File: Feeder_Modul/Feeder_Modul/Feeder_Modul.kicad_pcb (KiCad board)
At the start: 2 copper layers, 156.6 x 125.2 mm, 99 parts, among them J1 Conn_02x01, J101 Conn_02x01, J102 Conn_01x06_Male, J103 Conn_02x01, J104 Conn_02x01, J105 Conn_02x01, J106 USB_A, J107 Conn_02x07_Odd_Even, J108 Conn_02x01, J109 Conn_02x01, Q101 BC847, SW101 SW_Push, SW102 SW_Push, SW103 SW_Push, SW104 SW_Push, SW105 SW_Push, U1 TPS560430, U101 TPS560430, U102 STM32F105R8Tx, U103 M24C01-WMN, U104 EE-SX1350_PCB, U105 DRV8835, U107 SN65HVD230, Y101 48MHz

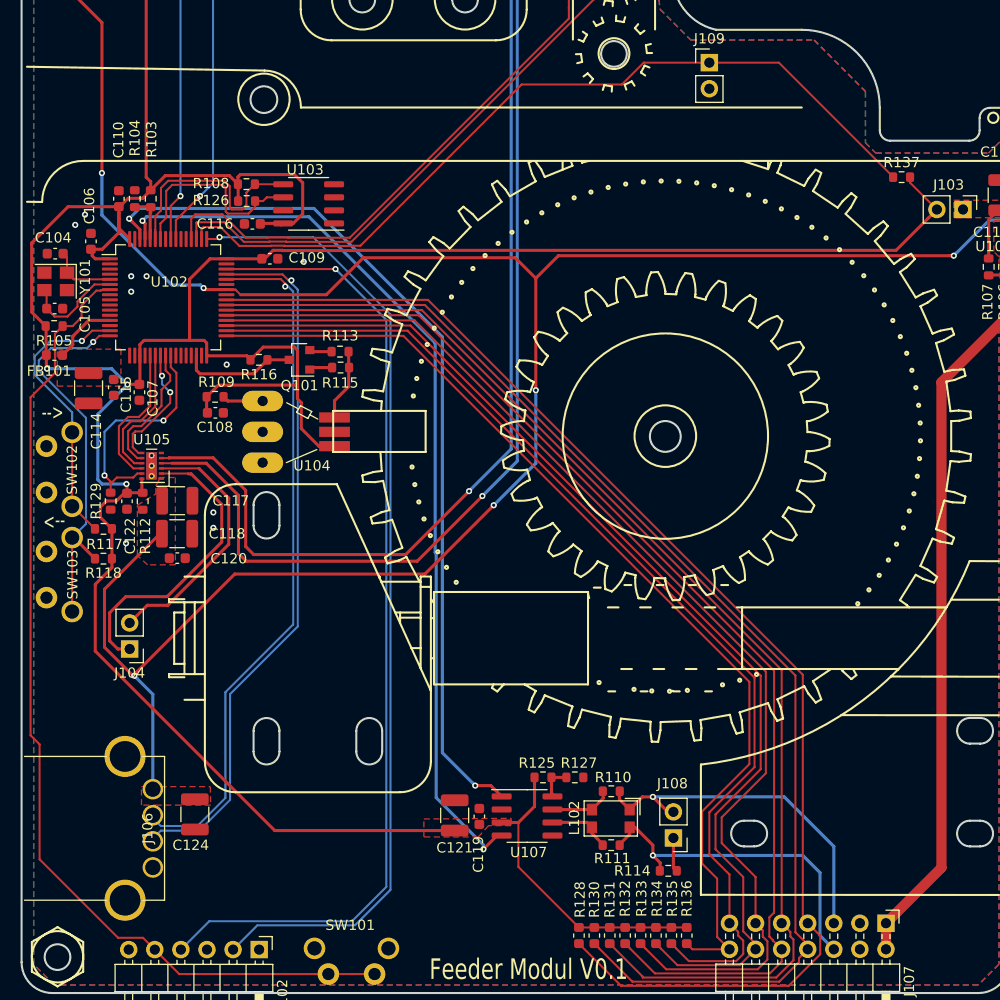
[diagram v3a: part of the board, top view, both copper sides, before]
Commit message: Controller Modul geroutet
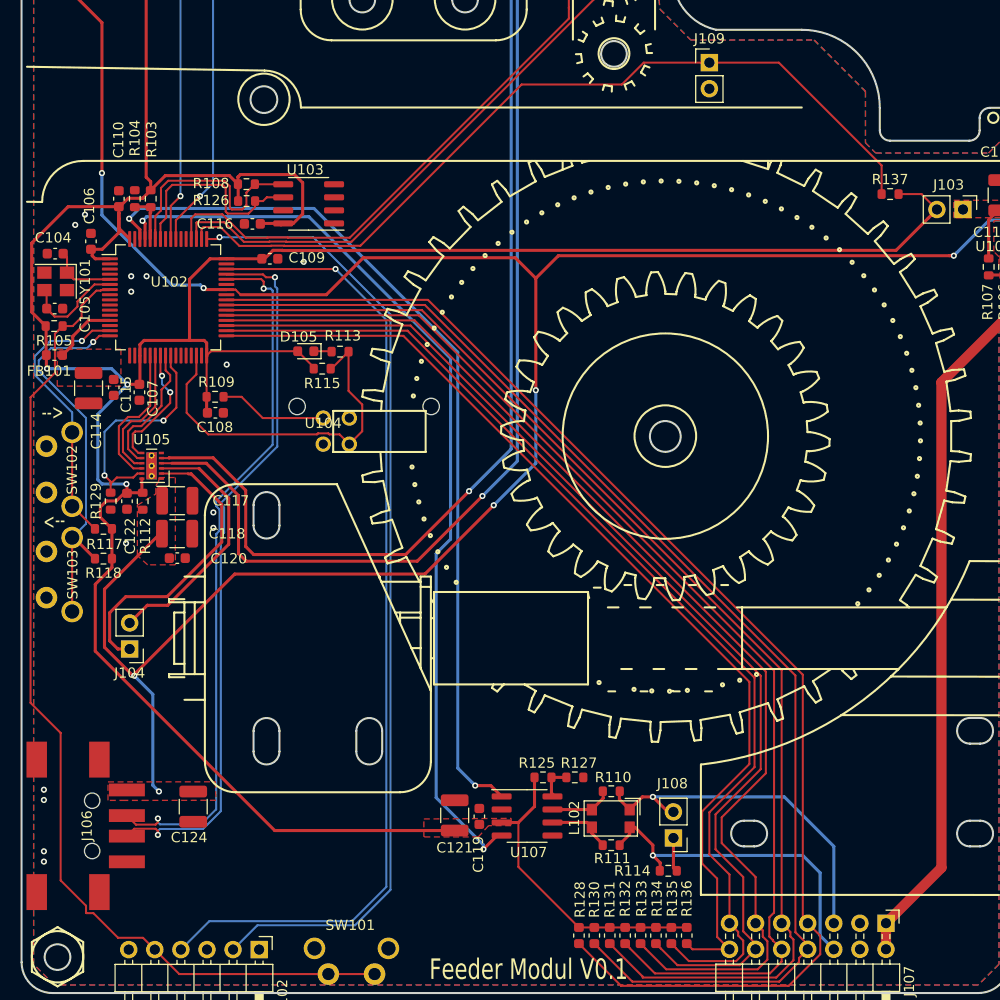
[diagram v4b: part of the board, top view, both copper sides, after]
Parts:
- removed Q101: BC847, Package_TO_SOT_SMD:SOT-23
- removed R116: 10K, Resistor_SMD:R_0603_1608Metric
- added D105: LED_Blue, LED_SMD:LED_0603_1608Metric, F.Cu at (91.5, 98.3)
- J106: value USB_A -> WE_629104190121; footprint ProjectFootprints:USB-A-Conn_LCSC -> ProjectFootprints:WE629104190121
- R113: value 10K -> 1K
- R115: value 1k -> 10K
- U104: value EE-SX1350_PCB -> TCST5250; footprint ProjectFootprints:EE-SX1350_90deg -> ProjectFootprints:TCST5250
- moved J106 5.91 mm to (70.7, 144.5)
- moved U104 2.75 mm to (93.2, 104.8)
- moved R137 1.99 mm to (148.4, 83.0)
- moved R115 1.79 mm to (93.1, 100.0), turned to 180 degrees
- moved C124 0.77 mm to (80.5, 142.7)
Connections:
- R113 pad 1: Net-(R113-Pad1) -> /ENC_OUT
- R113 pad 2: GND -> Net-(D105-Pad1)
- R115 pad 1: Net-(Q101-Pad1) -> /ENC_OUT
- R115 pad 2: Net-(R113-Pad1) -> +3V3
- U104 pad 2: (no net) -> GND
- U104 pad 4: +3V3 -> /ENC_OUT
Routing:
- net /ENC_OUT: track 11.2 -> 35.7 mm
- net +3V3: track 365.8 -> 350.6 mm
- net Net-(R113-Pad1): track 7.33 -> 0.00 mm
- net Net-(R109-Pad1): track 3.97 -> 10.6 mm
- net Net-(Q101-Pad1): track 2.30 -> 0.00 mm
- net GND: track 16.6 -> 14.4 mm, vias 10 -> 14
- net Net-(D105-Pad1): track 0.00 -> 1.74 mm
- net /USB_OTG+: track 69.2 -> 70.6 mm, vias 1 -> 2
- net /USB_OTG-: track 67.7 -> 69.0 mm, vias 1 -> 2
- net /TAPE_MICROBTN: track 81.2 -> 82.4 mm
- net /CAN1_RX: track 89.2 -> 90.4 mm
- net +5V: track 255.9 -> 255.6 mm, vias 6 -> 7

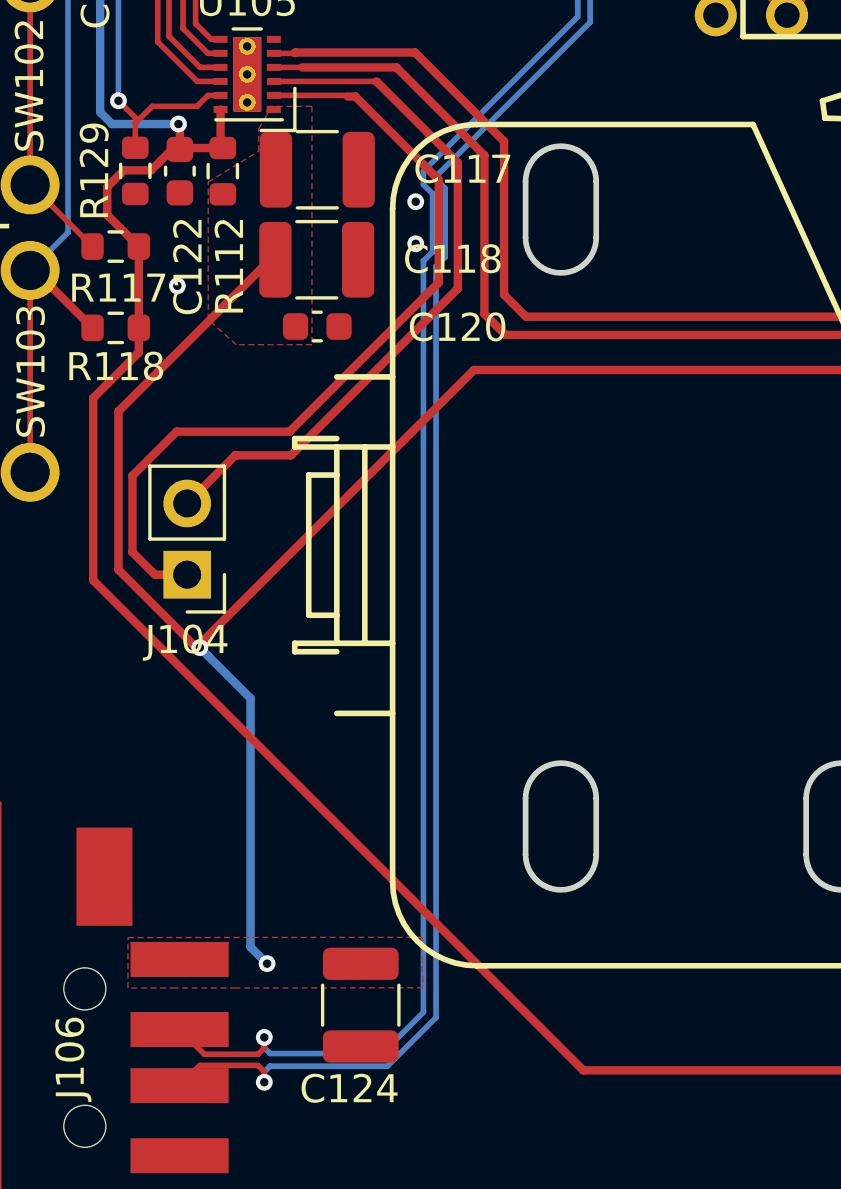
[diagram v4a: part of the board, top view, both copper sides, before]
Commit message: Leere Symbole mit leeren Footprints hinzugefügt für BOM export
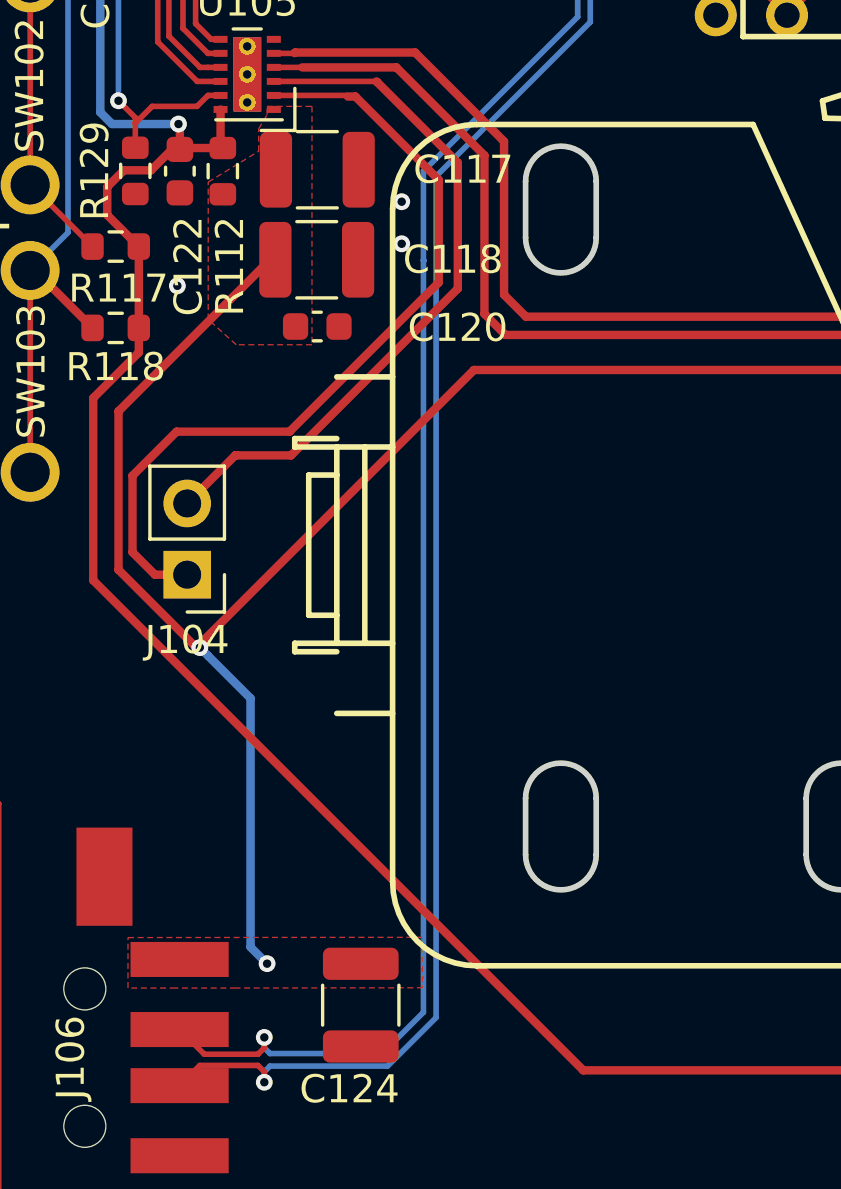
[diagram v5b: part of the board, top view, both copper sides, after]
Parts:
- added U106: Panasonic_ESE22, ProjectFootprints:Empty, F.Cu at (148.0, 138.0)
- added U108: N20_DC_Motor, ProjectFootprints:Empty, F.Cu at (148.0, 139.5)
- added U109: N20_DC_Motor, ProjectFootprints:Empty, F.Cu at (148.0, 141.0)
- R127: value 10K -> 1k
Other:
- board text added: "Empty Footprints for BOM"
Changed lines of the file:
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@@
   (general
     (thickness 1.6)
-    (drawings 1710)
-    (tracks 757)
+    (drawings 1711)
+    (tracks 751)
     (zones 0)
-    (modules 98)
+    (modules 101)
     (nets 66)
   )
@@
   )
   (setup
-    (last_trace_width 0.2)
+    (last_trace_width 0.3)
     (user_trace_width 0.2)
     (user_trace_width 0.3)
@@
     (add_net /MODE)
     (add_net /NRST)
+    (add_net /PA10)
     (add_net /PA13)
     (add_net /PA14)
     (add_net /PA6)
     (add_net /PA7)
+    (add_net /PA8)
     (add_net /PD0)
     (add_net /PD1)
@@
     (add_net "Net-(D104-Pad2)")
     (add_net "Net-(D105-Pad1)")
+    (add_net "Net-(J102-Pad6)")
     (add_net "Net-(J108-Pad1)")
     (add_net "Net-(L102-Pad1)")
@@
     (add_net "Net-(R125-Pad1)")
     (add_net "Net-(R3-Pad2)")
+    (add_net "Net-(U102-Pad10)")
+    (add_net "Net-(U102-Pad11)")
+    (add_net "Net-(U102-Pad14)")
+    (add_net "Net-(U102-Pad17)")
+    (add_net "Net-(U102-Pad2)")
+    (add_net "Net-(U102-Pad20)")
+    (add_net "Net-(U102-Pad26)")
+    (add_net "Net-(U102-Pad27)")
+    (add_net "Net-(U102-Pad28)")
+    (add_net "Net-(U102-Pad29)")
+    (add_net "Net-(U102-Pad3)")
+    (add_net "Net-(U102-Pad4)")
+    (add_net "Net-(U102-Pad53)")
+    (add_net "Net-(U102-Pad54)")
+    (add_net "Net-(U102-Pad57)")
+    (add_net "Net-(U102-Pad8)")
+    (add_net "Net-(U102-Pad9)")
+    (add_net "Net-(U107-Pad5)")
+  )
+  (module ProjectFootprints:Empty (layer F.Cu)
+    (at 148 141)
+    (fp_text reference U109 (at -0.5 -1.25) (layer F.SilkS) hide
+      (effects (font (size 1 1) (thickness 0.15)))
+    )
+    (fp_text value N20_DC_Motor (at -0.5 -1.5) (layer F.Fab)
+      (effects (font (size 1 1) (thickness 0.15)))
+    )
+    (fp_line (start 0 0) (end 1 0) (layer Dwgs.User) (width 0.12))
+  )
+  (module ProjectFootprints:Empty (layer F.Cu)
+    (at 148 139.5)
+    (fp_text reference U108 (at -0.5 -1.25) (layer F.SilkS) hide
+      (effects (font (size 1 1) (thickness 0.15)))
+    )
+    (fp_text value N20_DC_Motor (at -0.5 -1.5) (layer F.Fab)
+      (effects (font (size 1 1) (thickness 0.15)))
+    )
+    (fp_line (start 0 0) (end 1 0) (layer Dwgs.User) (width 0.12))
+  )
+  (module ProjectFootprints:Empty (layer F.Cu)
+    (at 148 138)
+    (fp_text reference U106 (at -0.5 -1.25) (layer F.SilkS) hide
+      (effects (font (size 1 1) (thickness 0.15)))
+    )
+    (fp_text value Panasonic_ESE22 (at -0.5 -1.5) (layer F.Fab)
+      (effects (font (size 1 1) (thickness 0.15)))
+    )
+    (fp_line (start 0 0) (end 1 0) (layer Dwgs.User) (width 0.12))
   )
   (module Resistor_SMD:R_0603_1608Metric (layer F.Cu)
@@
       (effects (font (size 1 1) (thickness 0.15)))
     )
-    (fp_text user %R (at 0 0) (layer F.Fab)
-      (effects (font (size 0.4 0.4) (thickness 0.06)))
-    )
     (fp_line (start -0.8 0.4125) (end -0.8 -0.4125) (layer F.Fab) (width 0.1))
     (fp_line (start -0.8 -0.4125) (end 0.8 -0.4125) (layer F.Fab) (width 0.1))
@@
     (fp_line (start 1.48 -0.73) (end 1.48 0.73) (layer F.CrtYd) (width 0.05))
     (fp_line (start 1.48 0.73) (end -1.48 0.73) (layer F.CrtYd) (width 0.05))
+    (fp_text user %R (at 0 0) (layer F.Fab)
+      (effects (font (size 0.4 0.4) (thickness 0.06)))
+    )
     (pad 2 smd roundrect (at 0.825 0 180) (size 0.8 0.95) (layers F.Cu F.Paste F.Mask) (roundrect_rratio 0.25)
       (net 6 +3V3))
@@
       (effects (font (size 1 1) (thickness 0.15)))
     )
+    (fp_line (start -6.55 6.9) (end 6.55 6.9) (layer Dwgs.User) (width 0.12))
     (fp_text user "Würth PCB Edge" (at -0.3 6.3 90) (layer Dwgs.User)
       (effects (font (size 1 1) (thickness 0.15)))
     )
-    (fp_line (start -6.55 6.9) (end 6.55 6.9) (layer Dwgs.User) (width 0.12))
     (pad 5 smd rect (at -6.45 5.4 270) (size 3.5 2) (layers F.Cu F.Paste F.Mask)
       (net 1 GND))
@@
       (effects (font (size 1 1) (thickness 0.15)))
     )
-    (fp_text value 10K (at 0 1.43) (layer F.Fab)
+    (fp_text value 1k (at 0 1.43) (layer F.Fab)
       (effects (font (size 1 1) (thickness 0.15)))
     )
@@
     )
   )
+  (gr_text "Empty Footprints \nfor BOM" (at 157 140) (layer Dwgs.User)
+    (effects (font (size 1 1) (thickness 0.15)))
+  )
   (gr_circle (center 126.5 106.6) (end 150.7 112.2) (layer Cmts.User) (width 0.15))
   (gr_text "Feeder Modul V0.1" (at 113.2 158.5) (layer F.SilkS)
@@
   (via (at 69.05 86) (size 0.6) (drill 0.3) (layers F.Cu B.Cu) (net 1))
   (via (at 74 117) (size 0.6) (drill 0.3) (layers F.Cu B.Cu) (net 1))
-  (via (at 82.5 114) (size 0.6) (drill 0.3) (layers F.Cu B.Cu) (net 1))
-  (via (at 82.5 115.5) (size 0.6) (drill 0.3) (layers F.Cu B.Cu) (net 1))
+  (via (at 82 114) (size 0.6) (drill 0.3) (layers F.Cu B.Cu) (net 1))
+  (via (at 82 115.5) (size 0.6) (drill 0.3) (layers F.Cu B.Cu) (net 1))
   (via (at 74.5 91) (size 0.6) (drill 0.3) (layers F.Cu B.Cu) (net 1))
   (via (at 76 91) (size 0.6) (drill 0.3) (layers F.Cu B.Cu) (net 1))
@@
   (segment (start 77.1 145.025) (end 76.875 144.8) (width 0.2) (layer F.Cu) (net 60))
   (segment (start 76.875 144.8) (end 74.8 144.8) (width 0.2) (layer F.Cu) (net 60))
-  (segment (start 81.4932 144.825) (end 77.3 144.825) (width 0.2) (layer B.Cu) (net 60))
-  (segment (start 83.225 116.299385) (end 83.225 143.0932) (width 0.2) (layer B.Cu) (net 60))
-  (segment (start 83.549992 115.974393) (end 83.225 116.299385) (width 0.2) (layer B.Cu) (net 60))
-  (segment (start 83.549992 113.525607) (end 83.549992 115.974393) (width 0.2) (layer B.Cu) (net 60))
-  (segment (start 83.225 143.0932) (end 81.4932 144.825) (width 0.2) (layer B.Cu) (net 60))
-  (segment (start 88.5 91.981801) (end 88.725 92.206801) (width 0.2) (layer B.Cu) (net 60))
-  (segment (start 88.725 107.5932) (end 83.225 113.0932) (width 0.2) (layer B.Cu) (net 60))
-  (segment (start 88.5 91.1) (end 88.5 91.981801) (width 0.2) (layer B.Cu) (net 60))
-  (segment (start 88.725 92.206801) (end 88.725 107.5932) (width 0.2) (layer B.Cu) (net 60))
-  (segment (start 77.3 144.825) (end 77.1 145.025) (width 0.2) (layer B.Cu) (net 60))
-  (segment (start 83.225 113.0932) (end 83.225 113.200615) (width 0.2) (layer B.Cu) (net 60))
-  (segment (start 83.225 113.200615) (end 83.549992 113.525607) (width 0.2) (layer B.Cu) (net 60))
   (segment (start 87.618199 91.1) (end 88.5 91.1) (width 0.2) (layer F.Cu) (net 60))
   (segment (start 87.343199 90.825) (end 87.618199 91.1) (width 0.2) (layer F.Cu) (net 60))
@@
   (segment (start 83.8 90.825) (end 87.343199 90.825) (width 0.2) (layer F.Cu) (net 60))
   (segment (start 77.1 145.025) (end 77.1 145.4) (width 0.2) (layer F.Cu) (net 60))
+  (segment (start 81.4932 144.825) (end 77.3 144.825) (width 0.2) (layer B.Cu) (net 60))
+  (segment (start 88.5 91.981801) (end 88.725 92.206801) (width 0.2) (layer B.Cu) (net 60))
+  (segment (start 83.225 113.0932) (end 83.225 143.0932) (width 0.2) (layer B.Cu) (net 60))
   (segment (start 77.1 145.025) (end 77.1 145.4) (width 0.2) (layer B.Cu) (net 60))
+  (segment (start 77.3 144.825) (end 77.1 145.025) (width 0.2) (layer B.Cu) (net 60))
+  (segment (start 88.5 91.1) (end 88.5 91.981801) (width 0.2) (layer B.Cu) (net 60))
+  (segment (start 88.725 92.206801) (end 88.725 107.5932) (width 0.2) (layer B.Cu) (net 60))
+  (segment (start 88.725 107.5932) (end 83.225 113.0932) (width 0.2) (layer B.Cu) (net 60))
+  (segment (start 83.225 143.0932) (end 81.4932 144.825) (width 0.2) (layer B.Cu) (net 60))
   (via (at 87.4 92.2) (size 0.6) (drill 0.3) (layers F.Cu B.Cu) (net 61))
   (via (at 77.1 143.8) (size 0.6) (drill 0.3) (layers F.Cu B.Cu) (net 61))
@@
   (segment (start 83.775 91.3) (end 83.8 91.275) (width 0.2) (layer F.Cu) (net 61))
   (segment (start 83.8 91.275) (end 87.156801 91.275) (width 0.2) (layer F.Cu) (net 61))
+  (segment (start 77.1 144.175) (end 77.1 143.8) (width 0.2) (layer F.Cu) (net 61))
   (segment (start 81.3068 144.375) (end 77.3 144.375) (width 0.2) (layer B.Cu) (net 61))
-  (segment (start 82.775 142.9068) (end 81.3068 144.375) (width 0.2) (layer B.Cu) (net 61))
-  (segment (start 82.775 116.100001) (end 82.775 142.9068) (width 0.2) (layer B.Cu) (net 61))
-  (segment (start 82.788001 116.100001) (end 82.775 116.100001) (width 0.2) (layer B.Cu) (net 61))
   (segment (start 77.3 144.375) (end 77.1 144.175) (width 0.2) (layer B.Cu) (net 61))
-  (segment (start 83.100001 113.711999) (end 83.100001 115.788001) (width 0.2) (layer B.Cu) (net 61))
+  (segment (start 82.788001 116.100001) (end 82.775 116.100001) (width 0.2) (layer B.Cu) (net 61))
   (segment (start 88.081801 92.2) (end 88.275 92.393199) (width 0.2) (layer B.Cu) (net 61))
-  (segment (start 82.775 112.9068) (end 82.775 113.386998) (width 0.2) (layer B.Cu) (net 61))
   (segment (start 87.4 92.2) (end 88.081801 92.2) (width 0.2) (layer B.Cu) (net 61))
-  (segment (start 83.100001 115.788001) (end 82.788001 116.100001) (width 0.2) (layer B.Cu) (net 61))
+  (segment (start 82.775 116.100001) (end 82.775 142.9068) (width 0.2) (layer B.Cu) (net 61))
   (segment (start 88.275 92.393199) (end 88.275 107.4068) (width 0.2) (layer B.Cu) (net 61))
-  (segment (start 88.275 107.4068) (end 82.775 112.9068) (width 0.2) (layer B.Cu) (net 61))
-  (segment (start 82.775 113.386998) (end 83.100001 113.711999) (width 0.2) (layer B.Cu) (net 61))
-  (segment (start 77.1 144.175) (end 77.1 143.8) (width 0.2) (layer F.Cu) (net 61))
   (segment (start 77.1 144.175) (end 77.1 143.8) (width 0.2) (layer B.Cu) (net 61))
+  (segment (start 82.775 116.087) (end 82.788001 116.100001) (width 0.2) (layer B.Cu) (net 61))
+  (segment (start 88.275 107.4068) (end 82.775 112.9068) (width 0.2) (layer B.Cu) (net 61))
+  (segment (start 82.775 142.9068) (end 81.3068 144.375) (width 0.2) (layer B.Cu) (net 61))
+  (segment (start 82.775 112.9068) (end 82.775 116.087) (width 0.2) (layer B.Cu) (net 61))
   (segment (start 86.56 82.045) (end 86.545 82.03) (width 0.2) (layer F.Cu) (net 62))
   (segment (start 89.305 82.045) (end 86.56 82.045) (width 0.2) (layer F.Cu) (net 62))
